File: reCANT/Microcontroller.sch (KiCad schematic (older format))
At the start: 22 parts, among them J2 Conn_02x08_Odd_Even, P1 SWD, SW1 SW_SPST, U2 LD1117S33TR, U3 STM32H743VITx

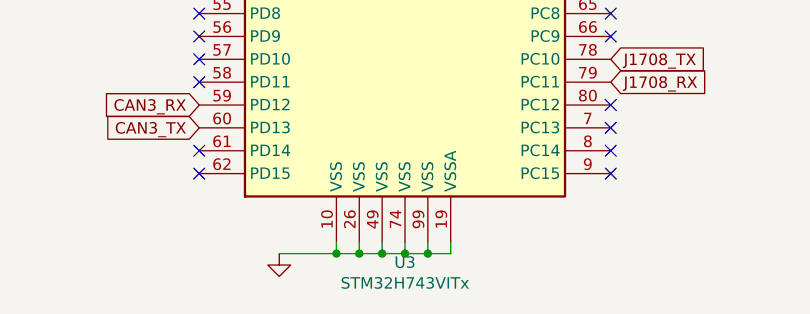
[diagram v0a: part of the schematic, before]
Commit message: Add LCSC part numbers for each component. Not that chipocalypse makes building this right now feasible...
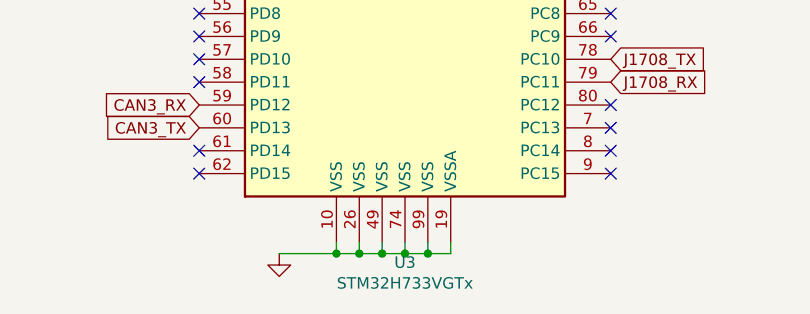
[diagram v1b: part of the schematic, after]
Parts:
- C10, C12, C13, C14, C2, C6, C7, C8, C9: LCSC (none) -> C49678
- C11: LCSC (none) -> C1779
- C15: LCSC (none) -> C28323
- C3: LCSC (none) -> C15850
- C4, C5: LCSC (none) -> C49217
- R6: LCSC (none) -> C17407
- R7: LCSC (none) -> C17414
- U2: LCSC (none) -> C86781
- U3: value STM32H743VITx -> STM32H733VGTx; LCSC (none) -> C730160
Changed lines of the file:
@@
 F 2 "Capacitor_SMD:C_0805_2012Metric" H 5600 1450 50  0001 C CNN
 F 3 "~" H 5600 1450 50  0001 C CNN
+F 4 "C49678" H 5600 1450 50  0001 C CNN "LCSC"
 	1    5600 1450
 	1    0    0    -1
@@
 F 2 "Capacitor_SMD:C_0805_2012Metric" H 8300 1450 50  0001 C CNN
 F 3 "~" H 8300 1450 50  0001 C CNN
+F 4 "C28323" H 8300 1450 50  0001 C CNN "LCSC"
 	1    8300 1450
 	1    0    0    -1
@@
 F 2 "Capacitor_SMD:C_0805_2012Metric" H 3938 2850 50  0001 C CNN
 F 3 "~" H 3900 3000 50  0001 C CNN
+F 4 "C49217" V 3900 3000 50  0001 C CNN "LCSC"
 	1    3900 3000
 	0    1    1    0
@@
 F 2 "Capacitor_SMD:C_0805_2012Metric" H 3938 2450 50  0001 C CNN
 F 3 "~" H 3900 2600 50  0001 C CNN
+F 4 "C49217" V 3900 2600 50  0001 C CNN "LCSC"
 	1    3900 2600
 	0    1    1    0
@@
 F 2 "Capacitor_SMD:C_0805_2012Metric" H 4200 2050 50  0001 C CNN
 F 3 "~" H 4200 2050 50  0001 C CNN
+F 4 "C49678" H 4200 2050 50  0001 C CNN "LCSC"
 	1    4200 2050
 	1    0    0    -1
@@
 F 2 "Resistor_SMD:R_0805_2012Metric" V 3530 2050 50  0001 C CNN
 F 3 "~" H 3600 2050 50  0001 C CNN
+F 4 "C17407" H 3600 2050 50  0001 C CNN "LCSC"
 	1    3600 2050
 	1    0    0    -1
@@
 AR Path="/6115D60F/611813C9" Ref="U3"  Part="1"
 F 0 "U3" H 5400 1811 50  0000 C CNN
-F 1 "STM32H743VITx" H 5400 1720 50  0000 C CNN
+F 1 "STM32H733VGTx" H 5400 1720 50  0000 C CNN
 F 2 "Package_QFP:LQFP-100_14x14mm_P0.5mm" H 4700 2100 50  0001 R CNN
-F 3 "http://www.st.com/st-web-ui/static/active/en/resource/technical/document/datasheet/DM00387108.pdf" H 5400 4700 50  0001 C CNN
+F 3 "https://www.st.com/resource/en/reference_manual/rm0468-stm32h723733-stm32h725735-and-stm32h730-value-line-advanced-armbased-32bit-mcus-stmicroelectronics.pdf" H 5400 4700 50  0001 C CNN
+F 4 "C730160" H 5400 4700 50  0001 C CNN "LCSC"
 	1    5400 4700
 	1    0    0    -1
@@
 F 2 "Package_TO_SOT_SMD:SOT-223" H 1450 3450 50  0001 C CNN
 F 3 "" H 1450 3350 50  0001 C CNN
+F 4 "C86781" H 1450 3350 50  0001 C CNN "LCSC"
 	1    1450 3350
 	1    0    0    -1
@@
 F 2 "Capacitor_SMD:C_0805_2012Metric" H 5150 1450 50  0001 C CNN
 F 3 "~" H 5150 1450 50  0001 C CNN
+F 4 "C49678" H 5150 1450 50  0001 C CNN "LCSC"
 	1    5150 1450
 	1    0    0    -1
@@
 F 2 "Capacitor_SMD:C_0805_2012Metric" H 4700 1450 50  0001 C CNN
 F 3 "~" H 4700 1450 50  0001 C CNN
+F 4 "C49678" H 4700 1450 50  0001 C CNN "LCSC"
 	1    4700 1450
 	1    0    0    -1
@@
 F 2 "Capacitor_SMD:C_0805_2012Metric" H 6950 1450 50  0001 C CNN
 F 3 "~" H 6950 1450 50  0001 C CNN
+F 4 "C49678" H 6950 1450 50  0001 C CNN "LCSC"
 	1    6950 1450
 	1    0    0    -1
@@
 F 2 "Capacitor_SMD:C_0805_2012Metric" H 7400 1450 50  0001 C CNN
 F 3 "~" H 7400 1450 50  0001 C CNN
+F 4 "C49678" H 7400 1450 50  0001 C CNN "LCSC"
 	1    7400 1450
 	1    0    0    -1
@@
 F 2 "Capacitor_SMD:C_0805_2012Metric" H 6050 1450 50  0001 C CNN
 F 3 "~" H 6050 1450 50  0001 C CNN
+F 4 "C49678" H 6050 1450 50  0001 C CNN "LCSC"
 	1    6050 1450
 	1    0    0    -1
@@
 F 2 "Capacitor_SMD:C_0805_2012Metric" H 7850 1450 50  0001 C CNN
 F 3 "~" H 7850 1450 50  0001 C CNN
+F 4 "C49678" H 7850 1450 50  0001 C CNN "LCSC"
 	1    7850 1450
 	1    0    0    -1
@@
 F 2 "Capacitor_SMD:C_0805_2012Metric" H 6500 1450 50  0001 C CNN
 F 3 "~" H 6500 1450 50  0001 C CNN
+F 4 "C1779" H 6500 1450 50  0001 C CNN "LCSC"
 	1    6500 1450
 	1    0    0    -1
@@
 F 3 "" H 9450 1350 30  0000 C CNN
 F 4 "MCR03ERTF5100" H 9450 1350 60  0001 C CNN "MPN"
+F 5 "C17414" V 9450 1350 50  0001 C CNN "LCSC"
 	1    9450 1350
 	1    0    0    -1
@@
 F 2 "Capacitor_SMD:C_0805_2012Metric" H 900 3550 50  0001 C CNN
 F 3 "~" H 900 3550 50  0001 C CNN
+F 4 "C49678" H 900 3550 50  0001 C CNN "LCSC"
 	1    900  3550
 	1    0    0    -1
@@
 F 2 "Capacitor_SMD:C_0805_2012Metric" H 2050 3550 50  0001 C CNN
 F 3 "~" H 2050 3550 50  0001 C CNN
+F 4 "C15850" H 2050 3550 50  0001 C CNN "LCSC"
 	1    2050 3550
 	1    0    0    -1
